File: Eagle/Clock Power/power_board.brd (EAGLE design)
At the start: 18 parts

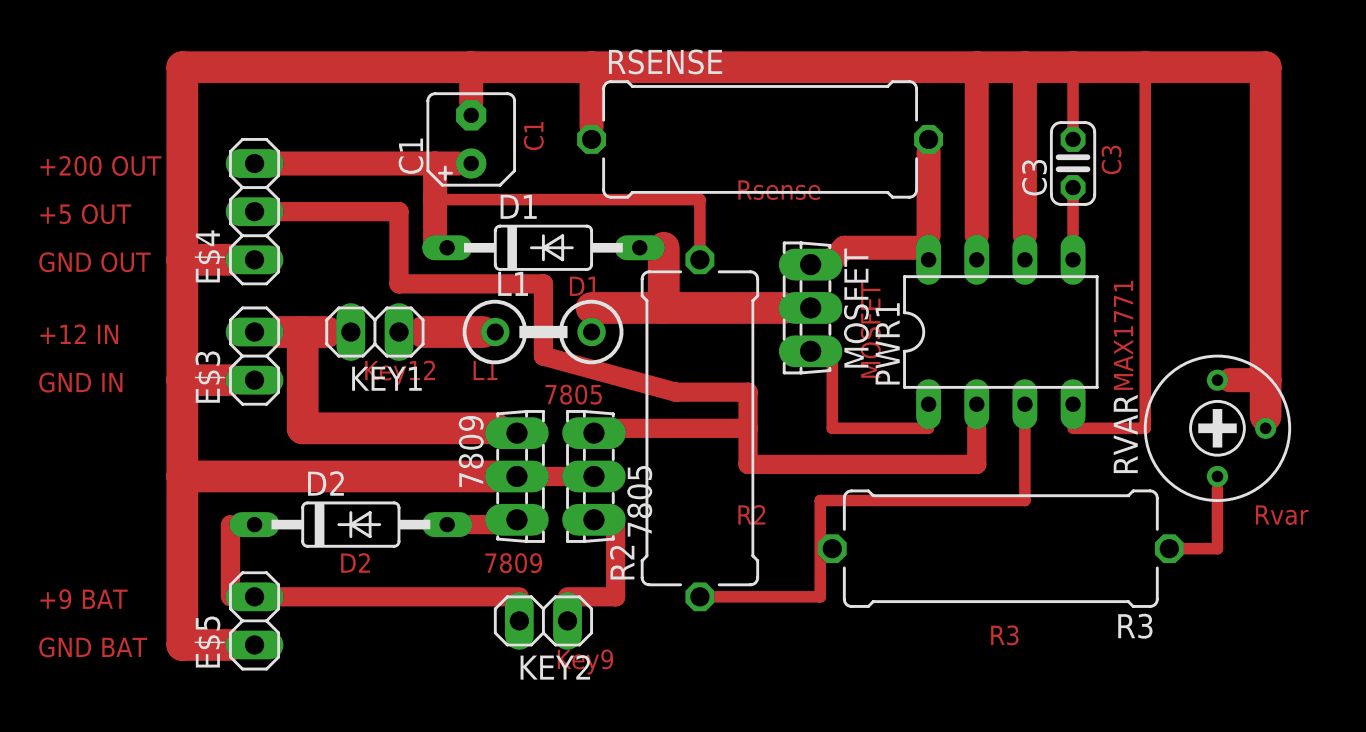
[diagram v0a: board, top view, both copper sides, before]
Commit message: Revert "Добавлены ключи, перемещен диод"
This reverts commit 3177369584cba4b2a743803ba8410bbd0b19749d.
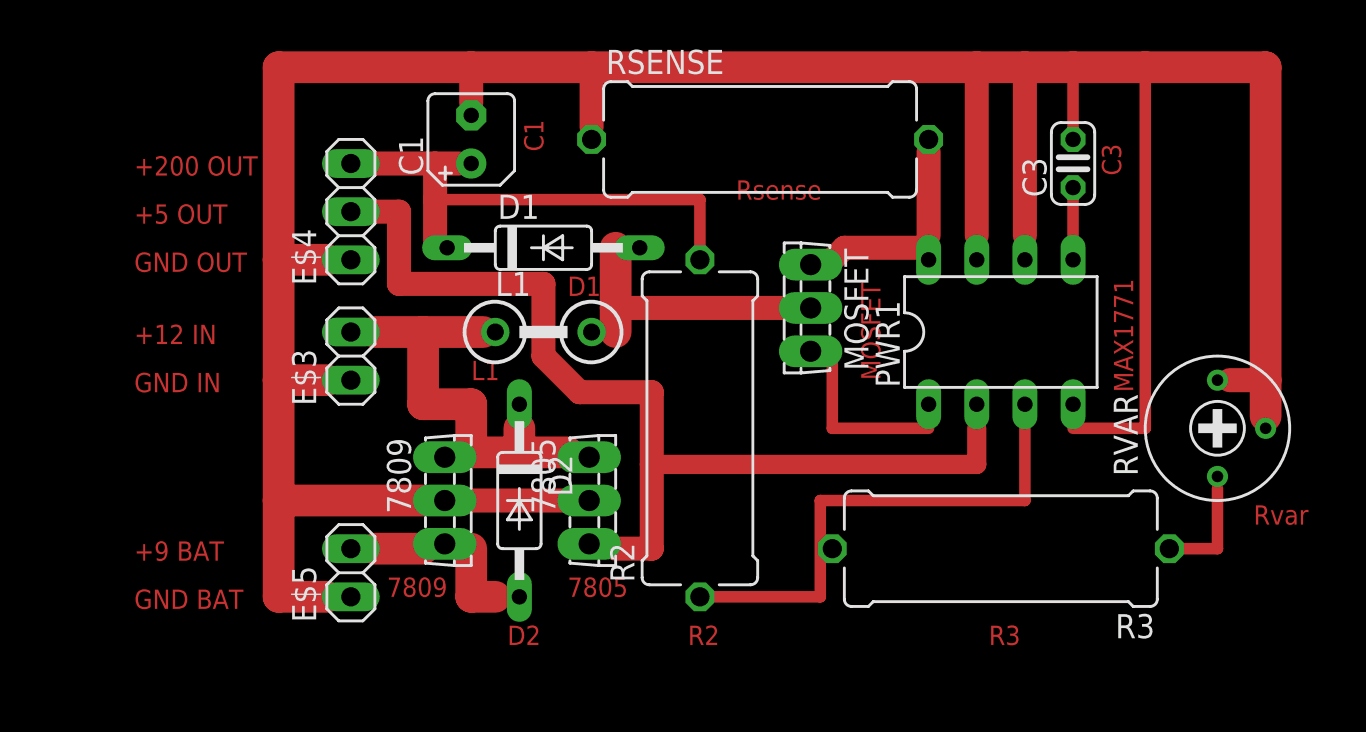
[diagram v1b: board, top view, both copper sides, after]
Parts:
- removed KEY1, KEY2: (no value), pinhead:1X02
- moved D2 8.98 mm to (14.0, 48.3), turned to 270 degrees
- moved E$5 5.68 mm to (5.08, 44.5)
- moved E$3 5.08 mm to (5.08, 55.9)
- moved E$4 5.08 mm to (5.08, 63.5)
- moved 7809 4.02 mm to (11.4, 48.3)
- moved 7805 2.84 mm to (19.1, 48.3), turned to 270 degrees
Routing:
- net GND: track 181.0 -> 164.5 mm
- net S$18: track 15.2 -> 0.00 mm
- net S$15: track 12.7 -> 0.00 mm
- net S$1: track 2.54 -> 14.6 mm
- net S$14: track 57.4 -> 52.2 mm
- net S$8: track 9.53 -> 4.45 mm
- net S$7: track 1.27 -> 5.08 mm
- net S$13: track 3.17 -> 0.00 mm
- net S$17: track 6.35 -> 3.81 mm
- net S$16: track 3.81 -> 6.35 mm
- net S$6: track 1.27 -> 2.54 mm
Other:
- board text removed: "Key12"
- board text removed: "Key9"

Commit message: Добавлены ключи, перемещен диод
Добавлены пины для подключения двухпозиционных переключателей,
разомкнута цепь между 7809 и 7805, диод D2 перемещен и теперь стоит
между 7809 и батареей
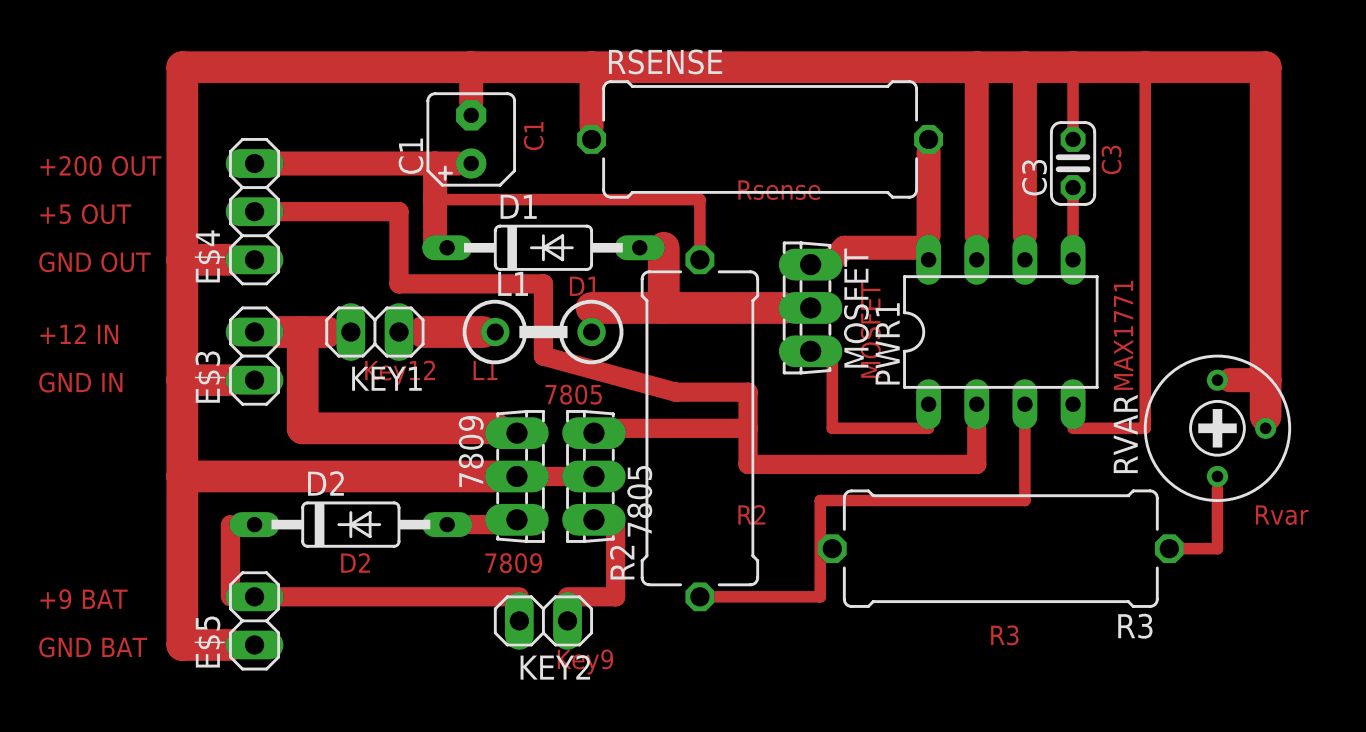
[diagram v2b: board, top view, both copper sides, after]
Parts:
- added KEY1, KEY2: (no value), pinhead:1X02
- moved D2 8.98 mm to (5.08, 47.0), turned to 0 degrees
- moved E$5 5.68 mm to (0.00, 41.9)
- moved E$3 5.08 mm to (0.00, 55.9)
- moved E$4 5.08 mm to (0.00, 63.5)
- moved 7809 4.02 mm to (15.2, 49.5)
- moved 7805 2.84 mm to (16.5, 49.5), turned to 90 degrees
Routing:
- net GND: track 164.5 -> 181.0 mm
- net S$18: track 0.00 -> 15.2 mm
- net S$15: track 0.00 -> 12.7 mm
- net S$1: track 14.6 -> 2.54 mm
- net S$14: track 52.2 -> 57.4 mm
- net S$8: track 4.45 -> 9.53 mm
- net S$7: track 5.08 -> 1.27 mm
- net S$13: track 0.00 -> 3.17 mm
- net S$17: track 3.81 -> 6.35 mm
- net S$16: track 6.35 -> 3.81 mm
- net S$6: track 2.54 -> 1.27 mm
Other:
- board text added: "Key12"
- board text added: "Key9"
